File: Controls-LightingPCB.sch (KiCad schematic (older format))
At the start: 12 parts, among them J1 MinionConn, U1 LTC6820, U2 HX1188FNL

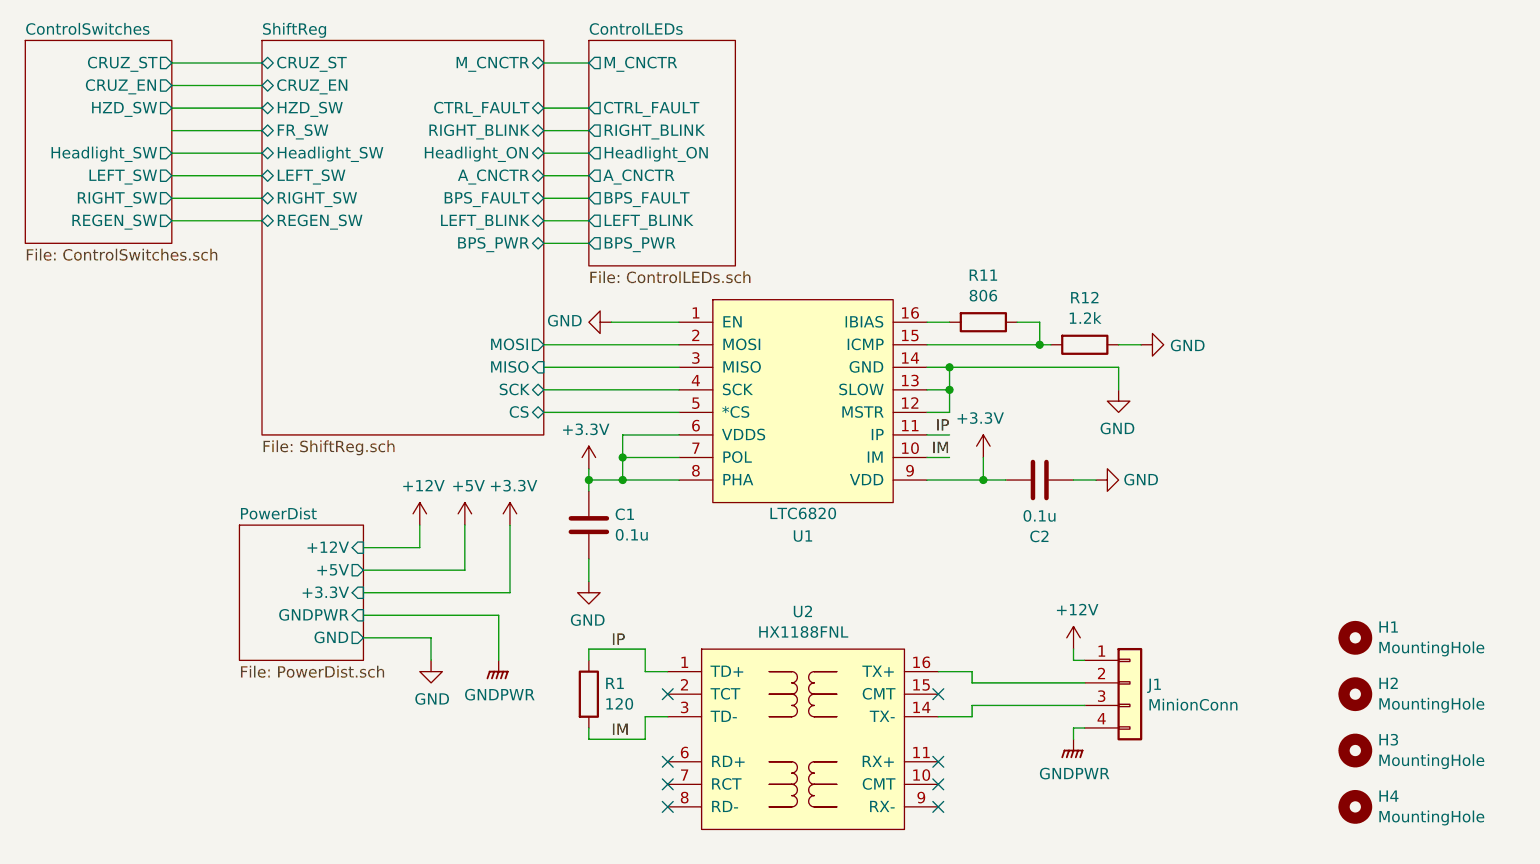
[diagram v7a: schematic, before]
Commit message: Updated schematic with changed F/W switch and BPS_PWR direct connection to MinionConn
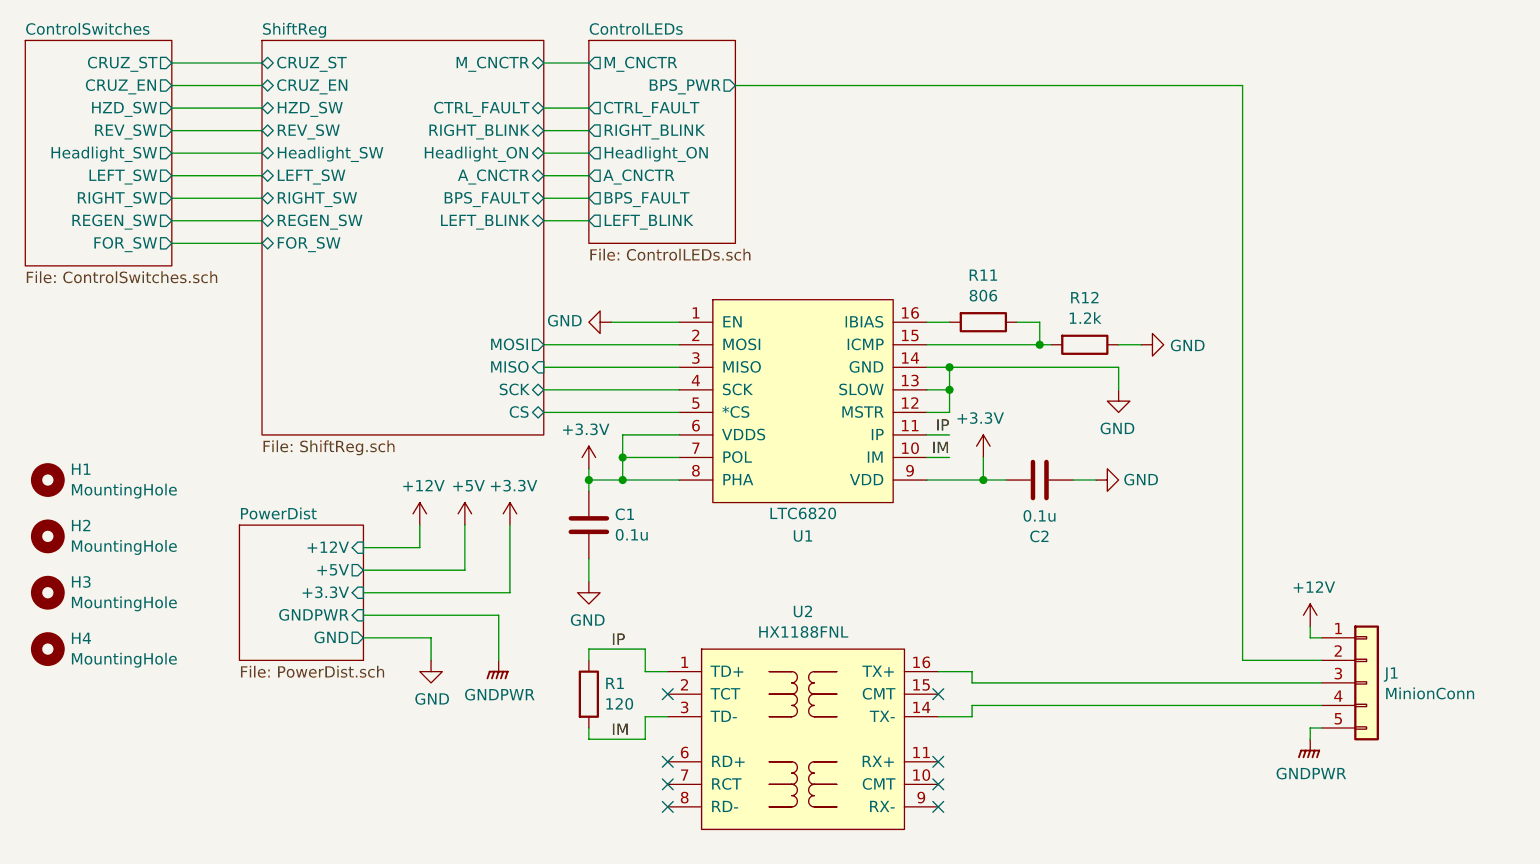
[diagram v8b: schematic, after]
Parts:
- removed J1: MinionConn, Connector_Molex:Molex_Micro-Fit_3.0_43650-0400_1x04_P3.00mm_Horizontal, symbol Connector_Generic:Conn_01x04
- added J1: MinionConn, Connector_Molex:Molex_Micro-Fit_3.0_43650-0500_1x05_P3.00mm_Horizontal, symbol Connector_Generic:Conn_01x05
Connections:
- net +12V: now also J1.1 (Pin_1)
- net ControlLEDs/BPS_PWR: now also J1.2 (Pin_2)
- net GNDPWR: now also J1.5 (Pin_5)
- net at U2.14 (TX-): now also J1.4 (Pin_4)
- net at U2.16 (TX+): now also J1.3 (Pin_3)
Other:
- moved on the sheet: H1, H2, H3, H4
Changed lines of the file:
@@
 $EndDescr
-Wire Wire Line
-	4250 2400 4050 2400
 Wire Wire Line
 	4050 2300 4250 2300
@@
 	4250 1600 4050 1600
 $Sheet
-S 4250 1500 650  1000
+S 4250 1500 650  900
 U 5F7A71E1
 F0 "ControlLEDs" 50
@@
 F7 "BPS_FAULT" O L 4250 2200 50
 F8 "LEFT_BLINK" O L 4250 2300 50
-F9 "BPS_PWR" O L 4250 2400 50
+F9 "BPS_PWR" O R 4900 1700 50
 $EndSheet
 $Sheet
@@
 F7 "BPS_FAULT" B R 4050 2200 50
 F8 "LEFT_BLINK" B R 4050 2300 50
-F9 "BPS_PWR" B R 4050 2400 50
-F10 "CRUZ_ST" B L 2800 1600 50
-F11 "CRUZ_EN" B L 2800 1700 50
-F12 "HZD_SW" B L 2800 1800 50
-F13 "FR_SW" B L 2800 1900 50
-F14 "Headlight_SW" B L 2800 2000 50
-F15 "LEFT_SW" B L 2800 2100 50
-F16 "RIGHT_SW" B L 2800 2200 50
-F17 "CS" B R 4050 3150 50
-F18 "SCK" B R 4050 3050 50
-F19 "MISO" I R 4050 2950 50
-F20 "MOSI" O R 4050 2850 50
-F21 "REGEN_SW" B L 2800 2300 50
+F9 "CRUZ_ST" B L 2800 1600 50
+F10 "CRUZ_EN" B L 2800 1700 50
+F11 "HZD_SW" B L 2800 1800 50
+F12 "Headlight_SW" B L 2800 2000 50
+F13 "LEFT_SW" B L 2800 2100 50
+F14 "RIGHT_SW" B L 2800 2200 50
+F15 "CS" B R 4050 3150 50
+F16 "SCK" B R 4050 3050 50
+F17 "MISO" I R 4050 2950 50
+F18 "MOSI" O R 4050 2850 50
+F19 "REGEN_SW" B L 2800 2300 50
+F20 "FOR_SW" B L 2800 2400 50
+F21 "REV_SW" B L 2800 1900 50
 $EndSheet
 $Comp
 L power:GNDPWR #PWR0103
 U 1 1 5F7E16B8
-P 6400 4600
-F 0 "#PWR0103" H 6400 4400 50  0001 C CNN
-F 1 "GNDPWR" H 6404 4446 50  0000 C CNN
-F 2 "" H 6400 4550 50  0001 C CNN
-F 3 "" H 6400 4550 50  0001 C CNN
-	1    6400 4600
+P 7450 4600
+F 0 "#PWR0103" H 7450 4400 50  0001 C CNN
+F 1 "GNDPWR" H 7454 4446 50  0000 C CNN
+F 2 "" H 7450 4550 50  0001 C CNN
+F 3 "" H 7450 4550 50  0001 C CNN
+	1    7450 4600
 	1    0    0    -1
 $EndComp
@@
 L power:+12V #PWR0104
 U 1 1 5F7E142C
-P 6400 4200
-F 0 "#PWR0104" H 6400 4050 50  0001 C CNN
-F 1 "+12V" H 6415 4373 50  0000 C CNN
-F 2 "" H 6400 4200 50  0001 C CNN
-F 3 "" H 6400 4200 50  0001 C CNN
-	1    6400 4200
+P 7450 4100
+F 0 "#PWR0104" H 7450 3950 50  0001 C CNN
+F 1 "+12V" H 7465 4273 50  0000 C CNN
+F 2 "" H 7450 4100 50  0001 C CNN
+F 3 "" H 7450 4100 50  0001 C CNN
+	1    7450 4100
 	1    0    0    -1
 $EndComp
@@
 IM
 $Sheet
-S 1750 1500 650  900
+S 1750 1500 650  1000
 U 5F78B3EB
 F0 "ControlSwitches" 50
@@
 F7 "RIGHT_SW" O R 2400 2200 50
 F8 "REGEN_SW" O R 2400 2300 50
+F9 "REV_SW" O R 2400 1900 50
+F10 "FOR_SW" O R 2400 2400 50
 $EndSheet
 Wire Wire Line
@@
 L Mechanical:MountingHole H4
 U 1 1 5F95A591
-P 7650 4900
-F 0 "H4" H 7750 4946 50  0000 L CNN
-F 1 "MountingHole" H 7750 4855 50  0000 L CNN
-F 2 "MountingHole:MountingHole_3mm" H 7650 4900 50  0001 C CNN
-F 3 "~" H 7650 4900 50  0001 C CNN
-	1    7650 4900
+P 1850 4200
+F 0 "H4" H 1950 4246 50  0000 L CNN
+F 1 "MountingHole" H 1950 4155 50  0000 L CNN
+F 2 "MountingHole:MountingHole_3mm" H 1850 4200 50  0001 C CNN
+F 3 "~" H 1850 4200 50  0001 C CNN
+	1    1850 4200
 	1    0    0    -1
 $EndComp
@@
 L Mechanical:MountingHole H3
 U 1 1 5F95AB20
-P 7650 4650
-F 0 "H3" H 7750 4696 50  0000 L CNN
-F 1 "MountingHole" H 7750 4605 50  0000 L CNN
-F 2 "MountingHole:MountingHole_3mm" H 7650 4650 50  0001 C CNN
-F 3 "~" H 7650 4650 50  0001 C CNN
-	1    7650 4650
+P 1850 3950
+F 0 "H3" H 1950 3996 50  0000 L CNN
+F 1 "MountingHole" H 1950 3905 50  0000 L CNN
+F 2 "MountingHole:MountingHole_3mm" H 1850 3950 50  0001 C CNN
+F 3 "~" H 1850 3950 50  0001 C CNN
+	1    1850 3950
 	1    0    0    -1
 $EndComp
@@
 L Mechanical:MountingHole H2
 U 1 1 5F95AF4E
-P 7650 4400
-F 0 "H2" H 7750 4446 50  0000 L CNN
-F 1 "MountingHole" H 7750 4355 50  0000 L CNN
-F 2 "MountingHole:MountingHole_3mm" H 7650 4400 50  0001 C CNN
-F 3 "~" H 7650 4400 50  0001 C CNN
-	1    7650 4400
+P 1850 3700
+F 0 "H2" H 1950 3746 50  0000 L CNN
+F 1 "MountingHole" H 1950 3655 50  0000 L CNN
+F 2 "MountingHole:MountingHole_3mm" H 1850 3700 50  0001 C CNN
+F 3 "~" H 1850 3700 50  0001 C CNN
+	1    1850 3700
 	1    0    0    -1
 $EndComp
@@
 L Mechanical:MountingHole H1
 U 1 1 5F95B613
-P 7650 4150
-F 0 "H1" H 7750 4196 50  0000 L CNN
-F 1 "MountingHole" H 7750 4105 50  0000 L CNN
-F 2 "MountingHole:MountingHole_3mm" H 7650 4150 50  0001 C CNN
-F 3 "~" H 7650 4150 50  0001 C CNN
-	1    7650 4150
+P 1850 3450
+F 0 "H1" H 1950 3496 50  0000 L CNN
+F 1 "MountingHole" H 1950 3405 50  0000 L CNN
+F 2 "MountingHole:MountingHole_3mm" H 1850 3450 50  0001 C CNN
+F 3 "~" H 1850 3450 50  0001 C CNN
+	1    1850 3450
 	1    0    0    -1
 $EndComp
@@
 Wire Wire Line
 	3500 3750 3500 3650
-$Comp
-L Connector_Generic:Conn_01x04 J1
-U 1 1 5FBD3314
-P 6650 4350
-F 0 "J1" H 6730 4342 50  0000 L CNN
-F 1 "MinionConn" H 6730 4251 50  0000 L CNN
-F 2 "Connector_Molex:Molex_Micro-Fit_3.0_43650-0400_1x04_P3.00mm_Horizontal" H 6650 4350 50  0001 C CNN
-F 3 "~" H 6650 4350 50  0001 C CNN
-	1    6650 4350
-	1    0    0    -1
-$EndComp
-Wire Wire Line
-	6400 4200 6400 4250
-Wire Wire Line
-	6400 4250 6450 4250
-Wire Wire Line
-	6450 4550 6400 4550
-Wire Wire Line
-	6400 4550 6400 4600
-Wire Wire Line
-	5950 4350 6450 4350
-Wire Wire Line
-	5950 4450 6450 4450
+Wire Wire Line
+	7450 4100 7450 4150
+Wire Wire Line
+	7450 4550 7450 4600
 Wire Wire Line
 	2400 2300 2800 2300
+Wire Wire Line
+	2400 2400 2800 2400
+$Comp
+L Connector_Generic:Conn_01x05 J1
+U 1 1 5FCAAC2B
+P 7700 4350
+F 0 "J1" H 7780 4392 50  0000 L CNN
+F 1 "MinionConn" H 7780 4301 50  0000 L CNN
+F 2 "Connector_Molex:Molex_Micro-Fit_3.0_43650-0500_1x05_P3.00mm_Horizontal" H 7700 4350 50  0001 C CNN
+F 3 "~" H 7700 4350 50  0001 C CNN
+	1    7700 4350
+	1    0    0    -1
+$EndComp
+Wire Wire Line
+	7450 4150 7500 4150
+Wire Wire Line
+	7500 4550 7450 4550
+Wire Wire Line
+	7500 4250 7150 4250
+Wire Wire Line
+	7150 4250 7150 1700
+Wire Wire Line
+	7150 1700 4900 1700
+Wire Wire Line
+	5950 4350 7500 4350
+Wire Wire Line
+	5950 4450 7500 4450
 $EndSCHEMATC
